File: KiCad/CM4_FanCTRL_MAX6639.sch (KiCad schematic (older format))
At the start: 14 parts

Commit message: generated part numbering
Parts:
- gave numbers to parts that had none: 14
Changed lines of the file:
@@
 	6200 4050 6550 4050
 $Comp
-L CM4_MATX:R R?
+L CM4_MATX:R R7
 U 1 1 5FE3BFBD
 P 6550 4350
-F 0 "R?" H 6620 4396 50  0000 L CNN
+F 0 "R7" H 6620 4396 50  0000 L CNN
 F 1 "R4.7k" H 6620 4305 50  0000 L CNN
 F 2 "CM4_MATX:R_0805_2012Metric_Pad1.20x1.40mm_HandSolder" V 6480 4350 50  0001 C CNN
@@
 $EndComp
 $Comp
-L CM4_MATX:R R?
+L CM4_MATX:R R32
 U 1 1 5FE3C88F
 P 7200 4350
-F 0 "R?" H 7270 4396 50  0000 L CNN
+F 0 "R32" H 7270 4396 50  0000 L CNN
 F 1 "R4.7k" H 7270 4305 50  0000 L CNN
 F 2 "CM4_MATX:R_0805_2012Metric_Pad1.20x1.40mm_HandSolder" V 7130 4350 50  0001 C CNN
@@
 $EndComp
 $Comp
-L CM4_MATX:R R?
+L CM4_MATX:R R34
 U 1 1 5FE3CE10
 P 7850 4350
-F 0 "R?" H 7920 4396 50  0000 L CNN
+F 0 "R34" H 7920 4396 50  0000 L CNN
 F 1 "R4.7k" H 7920 4305 50  0000 L CNN
 F 2 "CM4_MATX:R_0805_2012Metric_Pad1.20x1.40mm_HandSolder" V 7780 4350 50  0001 C CNN
@@
 $EndComp
 $Comp
-L CM4_MATX:R R?
+L CM4_MATX:R R35
 U 1 1 5FE3D2DA
 P 8500 4350
-F 0 "R?" H 8570 4396 50  0000 L CNN
+F 0 "R35" H 8570 4396 50  0000 L CNN
 F 1 "R4.7k" H 8570 4305 50  0000 L CNN
 F 2 "CM4_MATX:R_0805_2012Metric_Pad1.20x1.40mm_HandSolder" V 8430 4350 50  0001 C CNN
@@
 +3.3v
 $Comp
-L CM4_MATX:SolderJumper_3_Open JP?
+L CM4_MATX:SolderJumper_3_Open JP1
 U 1 1 5FE566B4
 P 4150 3000
-F 0 "JP?" V 4150 3067 50  0000 L CNN
+F 0 "JP1" V 4150 3067 50  0000 L CNN
 F 1 "SolderJumper_3_Open" H 4150 3110 50  0001 C CNN
 F 2 "CM4_MATX:SolderJumper-3_P2.0mm_Open_TrianglePad1.0x1.5mm_NumberLabels" H 4200 3200 50  0001 C CNN
@@
 	4150 3200 3550 3200
 $Comp
-L CM4_MATX:C C?
+L CM4_MATX:C C39
 U 1 1 5FE5258E
 P 3550 3000
-F 0 "C?" H 3665 3046 50  0000 L CNN
+F 0 "C39" H 3665 3046 50  0000 L CNN
 F 1 "C0.1u" H 3665 2955 50  0000 L CNN
 F 2 "CM4_MATX:C_0805_2012Metric_Pad1.18x1.45mm_HandSolder" H 3588 2850 50  0001 C CNN
@@
 +12v
 $Comp
-L CM4_MATX:SolderJumper_3_Open JP?
+L CM4_MATX:SolderJumper_3_Open JP2
 U 1 1 5FE6272C
 P 9500 850
-F 0 "JP?" H 9500 963 50  0000 C CNN
+F 0 "JP2" H 9500 963 50  0000 C CNN
 F 1 "SolderJumper_3_Open" H 9500 960 50  0001 C CNN
 F 2 "CM4_MATX:SolderJumper-3_P2.0mm_Open_TrianglePad1.0x1.5mm_NumberLabels" H 9550 1050 50  0001 C CNN
@@
 +3.3v
 $Comp
-L CM4_MATX:R R?
+L CM4_MATX:R R31
 U 1 1 5FE864CC
 P 7100 2300
-F 0 "R?" H 7170 2346 50  0000 L CNN
+F 0 "R31" H 7170 2346 50  0000 L CNN
 F 1 "R4.7k" H 7170 2255 50  0000 L CNN
 F 2 "CM4_MATX:R_0805_2012Metric_Pad1.20x1.40mm_HandSolder" V 7030 2300 50  0001 C CNN
@@
 $EndComp
 $Comp
-L CM4_MATX:R R?
+L CM4_MATX:R R33
 U 1 1 5FE86C3D
 P 7450 2300
-F 0 "R?" H 7520 2346 50  0000 L CNN
+F 0 "R33" H 7520 2346 50  0000 L CNN
 F 1 "R4.7k" H 7520 2255 50  0000 L CNN
 F 2 "CM4_MATX:R_0805_2012Metric_Pad1.20x1.40mm_HandSolder" V 7380 2300 50  0001 C CNN
@@
 $EndComp
 $Comp
-L CM4_MATX:R R?
+L CM4_MATX:R R5
 U 1 1 5FE87870
 P 6400 2300
-F 0 "R?" H 6470 2346 50  0000 L CNN
+F 0 "R5" H 6470 2346 50  0000 L CNN
 F 1 "R4.7k" H 6470 2255 50  0000 L CNN
 F 2 "CM4_MATX:R_0805_2012Metric_Pad1.20x1.40mm_HandSolder" V 6330 2300 50  0001 C CNN
@@
 $EndComp
 $Comp
-L CM4_MATX:R R?
+L CM4_MATX:R R30
 U 1 1 5FE88084
 P 6750 2300
-F 0 "R?" H 6820 2346 50  0000 L CNN
+F 0 "R30" H 6820 2346 50  0000 L CNN
 F 1 "R4.7k" H 6820 2255 50  0000 L CNN
 F 2 "CM4_MATX:R_0805_2012Metric_Pad1.20x1.40mm_HandSolder" V 6680 2300 50  0001 C CNN
@@
 	6400 2150 6400 2050
 $Comp
-L CM4_MATX:Fan_CPU_4pin M?
+L CM4_MATX:Fan_CPU_4pin M1
 U 1 1 5FE9485A
 P 8700 2000
-F 0 "M?" H 8858 2096 50  0000 L CNN
+F 0 "M1" H 8858 2096 50  0000 L CNN
 F 1 "Fan_CPU_4pin" H 8858 2005 50  0000 L CNN
 F 2 "CM4_MATX:FanPinHeader_1x04_P2.54mm_Vertical" H 8750 1460 50  0001 C CNN
@@
 $EndComp
 $Comp
-L CM4_MATX:Fan_CPU_4pin M?
+L CM4_MATX:Fan_CPU_4pin M2
 U 1 1 5FE9638A
 P 9500 2550
-F 0 "M?" H 9658 2646 50  0000 L CNN
+F 0 "M2" H 9658 2646 50  0000 L CNN
 F 1 "Fan_CPU_4pin" H 9658 2555 50  0000 L CNN
 F 2 "CM4_MATX:FanPinHeader_1x04_P2.54mm_Vertical" H 9550 2010 50  0001 C CNN
@@
 $EndComp
 $Comp
-L CM4_MATX:MAX6639ATE+ U?
+L CM4_MATX:MAX6639ATE+ U1
 U 1 1 5FE9AEED
 P 5700 3450
-F 0 "U?" H 5700 4415 50  0000 C CNN
+F 0 "U1" H 5700 4415 50  0000 C CNN
 F 1 "MAX6639ATE+" H 5700 4324 50  0000 C CNN
 F 2 "CM4_MATX:TQFN-16-1EP_5x5mm_P0.8mm_EP3.1x3.1mm" H 5750 4800 50  0001 C CNN
@@
 V_FAN
 $Comp
-L CM4_MATX:GND #PWR?
+L CM4_MATX:GND #PWR0201
 U 1 1 5FF29625
 P 4150 3400
-F 0 "#PWR?" H 4150 3150 50  0001 C CNN
+F 0 "#PWR0201" H 4150 3150 50  0001 C CNN
 F 1 "GND" H 4155 3227 50  0000 C CNN
 F 2 "" H 4150 3400 50  0001 C CNN
@@
 $EndComp
 $Comp
-L CM4_MATX:GND #PWR?
+L CM4_MATX:GND #PWR0202
 U 1 1 5FF2AB5B
 P 8700 2300
-F 0 "#PWR?" H 8700 2050 50  0001 C CNN
+F 0 "#PWR0202" H 8700 2050 50  0001 C CNN
 F 1 "GND" H 8705 2127 50  0000 C CNN
 F 2 "" H 8700 2300 50  0001 C CNN
@@
 $EndComp
 $Comp
-L CM4_MATX:GND #PWR?
+L CM4_MATX:GND #PWR0203
 U 1 1 5FF2C109
 P 9500 2850
-F 0 "#PWR?" H 9500 2600 50  0001 C CNN
+F 0 "#PWR0203" H 9500 2600 50  0001 C CNN
 F 1 "GND" H 9505 2677 50  0000 C CNN
 F 2 "" H 9500 2850 50  0001 C CNN

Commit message: updated printouts of schematics and pcb
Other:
- moved on the sheet: C39, M1, M2, R30, R31, R32, R33, R34, R35, R5, R7, U1

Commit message: changed solder jumper to pin jumper
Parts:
- removed JP1, JP2: SolderJumper_3_Open, CM4_MATX:SolderJumper-3_P2.0mm_Open_TrianglePad1.0x1.5mm_NumberLabels, symbol CM4_MATX:SolderJumper_3_Open
- added JP? (x2): Jumper_3_Open, CM4_MATX:PinHeader_1x03_P2.54mm_Vertical, symbol CM4_MATX:Jumper_3_Open
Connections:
- wire segments 71 -> 77
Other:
- moved on the sheet: C39
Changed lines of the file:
@@
 $EndDescr
 Wire Wire Line
-	4400 3800 3350 3800
-Connection ~ 3350 3800
-Wire Wire Line
 	4400 4000 3500 4000
-Wire Wire Line
-	4400 4200 3350 4200
-Wire Wire Line
-	3350 4200 3350 4400
-Connection ~ 3350 4200
 Wire Wire Line
 	4400 4400 4150 4400
@@
 Text HLabel 8200 5650 2    50   Input ~ 0
 +3.3v
-Wire Wire Line
-	3350 3800 3350 3550
 Text HLabel 3350 3550 0    50   Input ~ 0
 +3.3v
-$Comp
-L CM4_MATX:SolderJumper_3_Open JP1
-U 1 1 5FE566B4
-P 3350 4000
-F 0 "JP1" V 3350 4067 50  0000 L CNN
-F 1 "SolderJumper_3_Open" H 3350 4110 50  0001 C CNN
-F 2 "CM4_MATX:SolderJumper-3_P2.0mm_Open_TrianglePad1.0x1.5mm_NumberLabels" H 3400 4200 50  0001 C CNN
-F 3 "~" H 3350 4000 50  0001 C CNN
-	1    3350 4000
-	0    -1   -1   0
-$EndComp
-Wire Wire Line
-	3350 4200 2750 4200
-$Comp
-L CM4_MATX:C C39
-U 1 1 5FE5258E
-P 2750 4000
-F 0 "C39" H 2865 4046 50  0000 L CNN
-F 1 "C0.1u" H 2865 3955 50  0000 L CNN
-F 2 "CM4_MATX:C_0805_2012Metric_Pad1.18x1.45mm_HandSolder" H 2788 3850 50  0001 C CNN
-F 3 "~" H 2750 4000 50  0001 C CNN
-	1    2750 4000
-	1    0    0    -1
-$EndComp
-Wire Wire Line
-	2750 3850 2750 3800
-Wire Wire Line
-	2750 3800 3350 3800
-Wire Wire Line
-	2750 4150 2750 4200
-Text HLabel 8350 1850 0    50   Input ~ 0
-+5v
-Text HLabel 9050 1850 2    50   Input ~ 0
+Text HLabel 9100 1850 2    50   Input ~ 0
 +12v
-$Comp
-L CM4_MATX:SolderJumper_3_Open JP2
-U 1 1 5FE6272C
-P 8700 1850
-F 0 "JP2" H 8700 1963 50  0000 C CNN
-F 1 "SolderJumper_3_Open" H 8700 1960 50  0001 C CNN
-F 2 "CM4_MATX:SolderJumper-3_P2.0mm_Open_TrianglePad1.0x1.5mm_NumberLabels" H 8750 2050 50  0001 C CNN
-F 3 "~" H 8700 1850 50  0001 C CNN
-	1    8700 1850
-	1    0    0    -1
-$EndComp
-Wire Wire Line
-	8350 1850 8500 1850
-Wire Wire Line
-	8900 1850 9050 1850
 Text Label 3850 3800 0    50   ~ 0
 +3.3v
@@
 Connection ~ 7900 2500
 Connection ~ 6650 3050
-Text Notes 1400 4600 0    50   ~ 0
+Text Notes 3200 4650 2    50   ~ 0
 Addressselection by connecting jumperpads:\n2 and 3    ->   5Eh \nnone       ->   5Ch\n2 and 1    ->   58h
+$Comp
+L CM4_MATX:C C39
+U 1 1 5FE5258E
+P 2300 4000
+F 0 "C39" H 2415 4046 50  0000 L CNN
+F 1 "C0.1u" H 2415 3955 50  0000 L CNN
+F 2 "CM4_MATX:C_0805_2012Metric_Pad1.18x1.45mm_HandSolder" H 2338 3850 50  0001 C CNN
+F 3 "~" H 2300 4000 50  0001 C CNN
+	1    2300 4000
+	1    0    0    -1
+$EndComp
+$Comp
+L CM4_MATX:Jumper_3_Open JP?
+U 1 1 5FE5CBBB
+P 3350 4000
+F 0 "JP?" V 3396 4087 50  0000 L CNN
+F 1 "Jumper_3_Open" V 3305 4087 50  0000 L CNN
+F 2 "CM4_MATX:PinHeader_1x03_P2.54mm_Vertical" H 3350 4000 50  0001 C CNN
+F 3 "~" H 3350 4000 50  0001 C CNN
+	1    3350 4000
+	0    -1   -1   0
+$EndComp
+Wire Wire Line
+	4400 4200 3750 4200
+Wire Wire Line
+	3750 4200 3750 4300
+Wire Wire Line
+	3750 4300 3350 4300
+Wire Wire Line
+	3350 4300 3350 4250
+Wire Wire Line
+	3350 4300 3350 4400
+Connection ~ 3350 4300
+Wire Wire Line
+	4400 3800 3750 3800
+Wire Wire Line
+	3750 3800 3750 3700
+Wire Wire Line
+	3750 3700 3350 3700
+Wire Wire Line
+	3350 3700 3350 3750
+Wire Wire Line
+	3350 3700 3350 3550
+Connection ~ 3350 3700
+Wire Wire Line
+	3350 3700 2300 3700
+Wire Wire Line
+	2300 3700 2300 3850
+Wire Wire Line
+	2300 4150 2300 4300
+Wire Wire Line
+	2300 4300 3350 4300
+Text HLabel 8300 1850 0    50   Input ~ 0
++5v
+Wire Wire Line
+	8950 1850 9100 1850
+Wire Wire Line
+	8300 1850 8450 1850
+$Comp
+L CM4_MATX:Jumper_3_Open JP?
+U 1 1 5FE7DA5B
+P 8700 1850
+F 0 "JP?" H 8700 2074 50  0000 C CNN
+F 1 "Jumper_3_Open" H 8700 1983 50  0000 C CNN
+F 2 "CM4_MATX:PinHeader_1x03_P2.54mm_Vertical" H 8700 1850 50  0001 C CNN
+F 3 "~" H 8700 1850 50  0001 C CNN
+	1    8700 1850
+	1    0    0    -1
+$EndComp
 $EndSCHEMATC

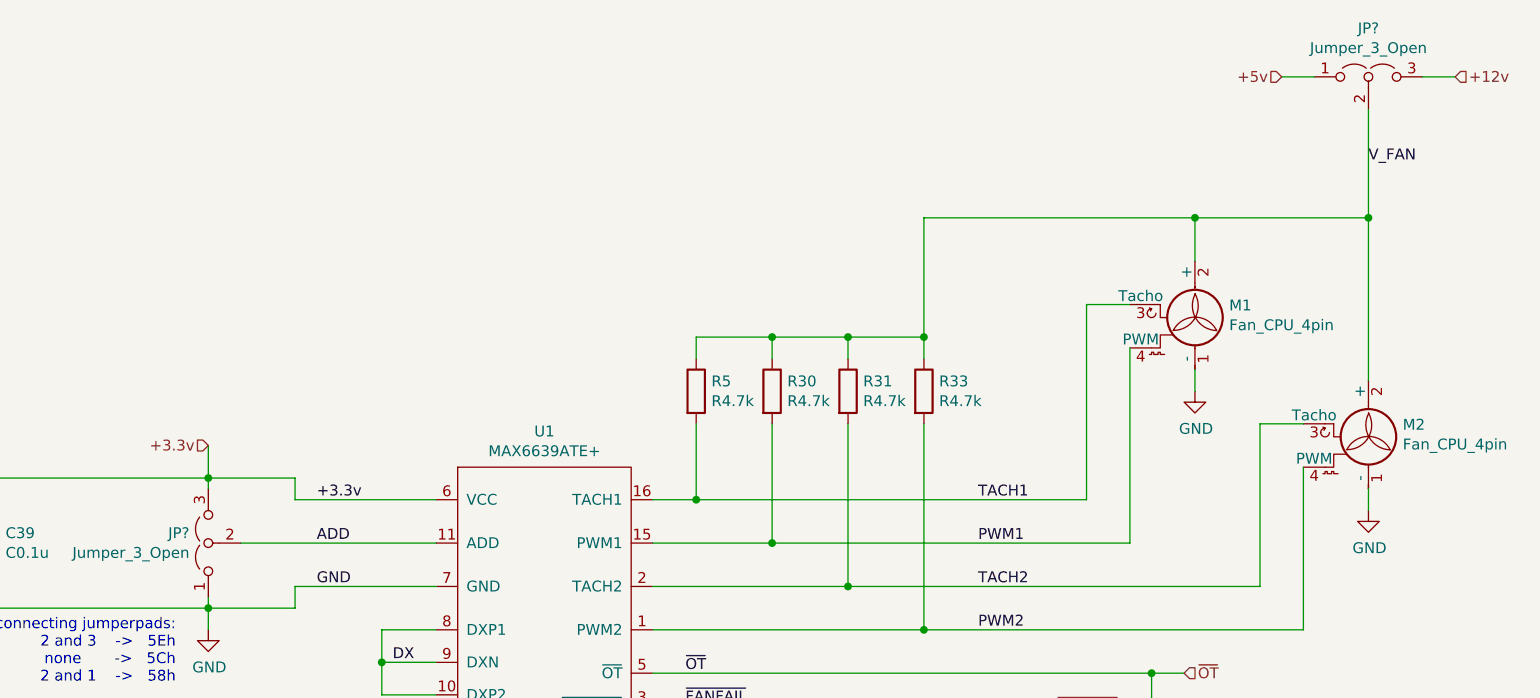
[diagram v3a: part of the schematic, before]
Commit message: added jumper descriptions
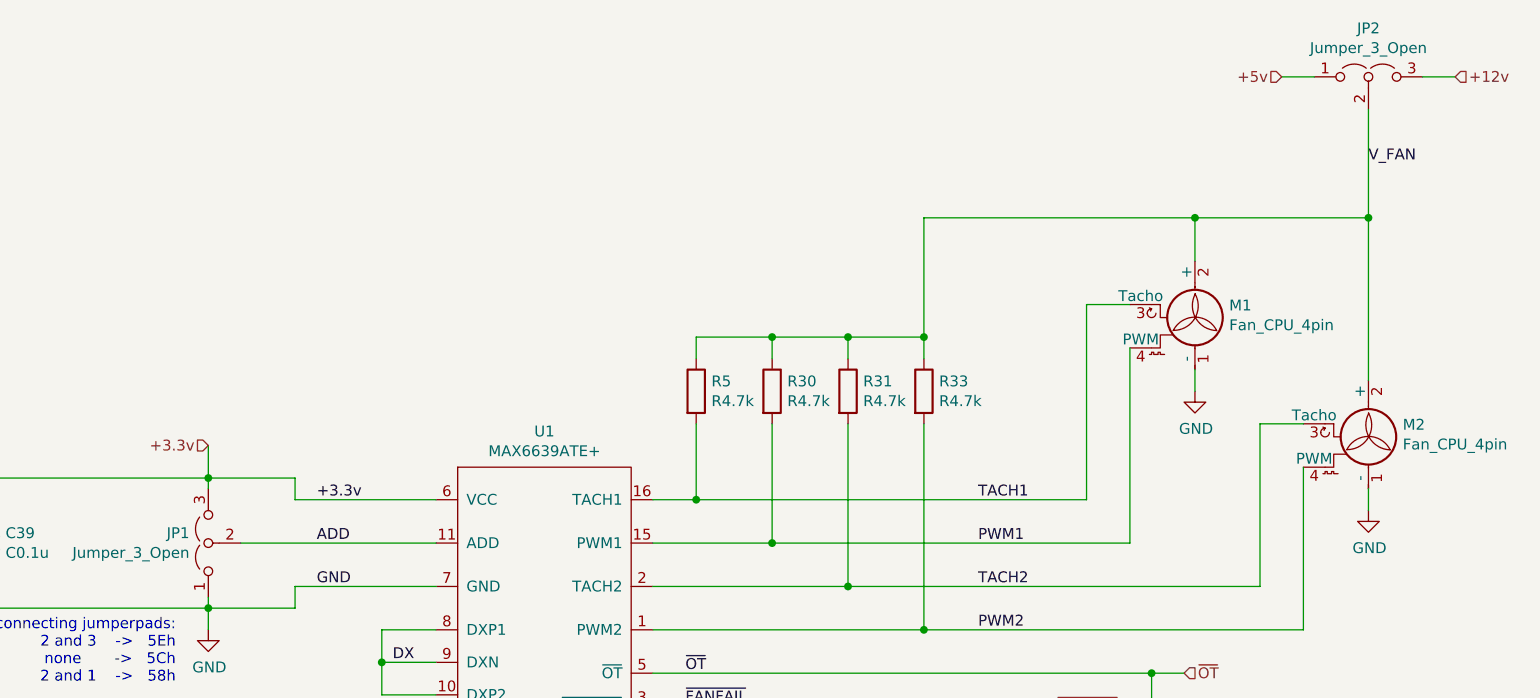
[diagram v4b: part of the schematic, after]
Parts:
- gave numbers to parts that had none: 2
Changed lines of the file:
@@
 $EndComp
 $Comp
-L CM4_MATX:Jumper_3_Open JP?
+L CM4_MATX:Jumper_3_Open JP1
 U 1 1 5FE5CBBB
 P 3350 4000
-F 0 "JP?" V 3396 4087 50  0000 L CNN
+F 0 "JP1" V 3396 4087 50  0000 L CNN
 F 1 "Jumper_3_Open" V 3305 4087 50  0000 L CNN
 F 2 "CM4_MATX:PinHeader_1x03_P2.54mm_Vertical" H 3350 4000 50  0001 C CNN
@@
 	8300 1850 8450 1850
 $Comp
-L CM4_MATX:Jumper_3_Open JP?
+L CM4_MATX:Jumper_3_Open JP2
 U 1 1 5FE7DA5B
 P 8700 1850
-F 0 "JP?" H 8700 2074 50  0000 C CNN
+F 0 "JP2" H 8700 2074 50  0000 C CNN
 F 1 "Jumper_3_Open" H 8700 1983 50  0000 C CNN
 F 2 "CM4_MATX:PinHeader_1x03_P2.54mm_Vertical" H 8700 1850 50  0001 C CNN
